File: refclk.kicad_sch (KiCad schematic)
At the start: 57 parts, among them J10 U.FL-R, Q1 PMOS Si2343DS, Q2 MMBT3904, Q3 PMOS Si2343DS, U14 LP5907MFX-3.3, U16 TLV3501, U18 NC7SV157, U19 74LVC2G14, U20 Si5351A, U21 NC7SV157, U22 SN65LVDS1, X1 TCXO-27M

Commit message: Bring over ringof/dev (tranche 2, stage 1): design, library, 3D, board CI & docs
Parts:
- C62, C65: footprint TIS_Footprints:PAD_0603 -> Library:C_0603
- C63, C64, C66, C67, C68, C69, C70, C71, C72, C73, C74, C75, C76: footprint TIS_Footprints:C_0603 -> Library:C_0603
- C78: footprint TIS_Footprints:PAD_0603 -> Library:C_0603; symbol capacitors:C-8.2p-0603 -> Library:C-8.2p-0603
- J10: footprint TIS_Footprints:HRS_U.FL-R-SMT(01) -> Library:HRS_U.FL-R-SMT(01)
- L15, L16, L17: footprint TIS_Footprints:0603 -> Library:0603
- Q1, Q2, Q3, U15, U17: footprint TIS_Footprints:SOT-23 -> Library:SOT-23
- R41, R42, R43, R44, R45, R46, R47, R48, R49, R50, R51, R52, R53, R54, R55, R56, R57, R60: footprint TIS_Footprints:PAD_0603 -> Library:PAD_0603
- R61: footprint TIS_Footprints:PAD_0603 -> Library:PAD_0603; symbol resistors:R-100-0603 -> Library:R-100-0603
- TP15, TP16, TP17, TP18, TP19: footprint TIS_Footprints:TP -> Library:TP; now not fitted
- U14, U22: footprint TIS_Footprints:SOT-23-5 -> Library:SOT-23-5
- U16: footprint TIS_Footprints:SOT-23-6 -> Library:SOT-23-6
- U18, U21: footprint TIS_Footprints:SC-70-6 -> Library:SC-70-6
- U19: footprint TIS_Footprints:SC-70-6_rot90 -> Library:SC-70-6_rot90
- U20: footprint TIS_Footprints:MSOP-10_W3mm -> Library:MSOP-10_W3mm
- X1: footprint TIS_Footprints:TCXO-3225 -> Library:TCXO-3225
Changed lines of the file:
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@@
 			)
 		)
-		(property "Footprint" "TIS_Footprints:SOT-23"
+		(property "Footprint" "Library:SOT-23"
 			(at 109.855 34.29 0)
 			(hide yes)
@@
 			)
 		)
-		(property "Footprint" "TIS_Footprints:SOT-23-6"
+		(property "Footprint" "Library:SOT-23-6"
 			(at 111.76 88.9 0)
 			(hide yes)
@@
 		(on_board yes)
 		(in_pos_files yes)
-		(dnp no)
+		(dnp yes)
 		(property "Reference" "TP17"
 			(at 90.3732 168.148 0)
@@
 			)
 		)
-		(property "Footprint" "TIS_Footprints:TP"
+		(property "Footprint" "Library:TP"
 			(at 85.09 161.29 0)
 			(hide yes)
@@
 			)
 		)
-		(property "Footprint" "TIS_Footprints:C_0603"
+		(property "Footprint" "Library:C_0603"
 			(at 138.176 39.878 0)
 			(hide yes)
@@
 			)
 		)
-		(property "Footprint" "TIS_Footprints:SOT-23-5"
+		(property "Footprint" "Library:SOT-23-5"
 			(at 234.95 52.07 0)
 			(hide yes)
@@
 			)
 		)
-		(property "Footprint" "TIS_Footprints:HRS_U.FL-R-SMT(01)"
+		(property "Footprint" "Library:HRS_U.FL-R-SMT(01)"
 			(at 219.71 10.16 0)
 			(hide yes)
@@
 			)
 		)
-		(property "Footprint" "TIS_Footprints:TCXO-3225"
+		(property "Footprint" "Library:TCXO-3225"
 			(at 153.67 58.42 0)
 			(hide yes)
@@
 			)
 		)
-		(property "Footprint" "TIS_Footprints:0603"
+		(property "Footprint" "Library:0603"
 			(at 128.778 27.178 0)
 			(hide yes)
@@
 			)
 		)
-		(property "Footprint" "TIS_Footprints:PAD_0603"
+		(property "Footprint" "Library:PAD_0603"
 			(at 173.736 120.904 90)
 			(hide yes)
@@
 			)
 		)
-		(property "Footprint" "TIS_Footprints:C_0603"
+		(property "Footprint" "Library:C_0603"
 			(at 189.484 79.502 0)
 			(hide yes)
@@
 			)
 		)
-		(property "Footprint" "TIS_Footprints:C_0603"
+		(property "Footprint" "Library:C_0603"
 			(at 205.994 141.732 0)
 			(hide yes)
@@
 	)
 	(symbol
-		(lib_id "resistors:R-100-0603")
+		(lib_id "Library:R-100-0603")
 		(at 246.38 29.21 0)
 		(unit 1)
@@
 			)
 		)
-		(property "Footprint" "TIS_Footprints:PAD_0603"
+		(property "Footprint" "Library:PAD_0603"
 			(at 247.396 29.464 90)
 			(hide yes)
@@
 			)
 		)
-		(property "Footprint" "TIS_Footprints:SOT-23"
+		(property "Footprint" "Library:SOT-23"
 			(at 58.928 123.317 0)
 			(hide yes)
@@
 			)
 		)
-		(property "Footprint" "TIS_Footprints:C_0603"
+		(property "Footprint" "Library:C_0603"
 			(at 232.156 112.268 0)
 			(hide yes)
@@
 			)
 		)
-		(property "Footprint" "TIS_Footprints:C_0603"
+		(property "Footprint" "Library:C_0603"
 			(at 241.554 49.022 0)
 			(hide yes)
@@
 			)
 		)
-		(property "Footprint" "TIS_Footprints:SOT-23"
+		(property "Footprint" "Library:SOT-23"
 			(at 132.588 141.097 0)
 			(hide yes)
@@
 			)
 		)
-		(property "Footprint" "TIS_Footprints:PAD_0603"
+		(property "Footprint" "Library:PAD_0603"
 			(at 218.186 90.424 90)
 			(hide yes)
@@
 			)
 		)
-		(property "Footprint" "TIS_Footprints:PAD_0603"
+		(property "Footprint" "Library:PAD_0603"
 			(at 232.156 156.464 90)
 			(hide yes)
@@
 			)
 		)
-		(property "Footprint" "TIS_Footprints:C_0603"
+		(property "Footprint" "Library:C_0603"
 			(at 254.254 144.272 0)
 			(hide yes)
@@
 		(on_board yes)
 		(in_pos_files yes)
-		(dnp no)
+		(dnp yes)
 		(property "Reference" "TP15"
 			(at 29.718 106.426 0)
@@
 			)
 		)
-		(property "Footprint" "TIS_Footprints:TP"
+		(property "Footprint" "Library:TP"
 			(at 26.67 100.33 0)
 			(hide yes)
@@
 			)
 		)
-		(property "Footprint" "TIS_Footprints:0603"
+		(property "Footprint" "Library:0603"
 			(at 222.758 99.568 0)
 			(hide yes)
@@
 			)
 		)
-		(property "Footprint" "TIS_Footprints:C_0603"
+		(property "Footprint" "Library:C_0603"
 			(at 131.318 131.064 0)
 			(hide yes)
@@
 			)
 		)
-		(property "Footprint" "TIS_Footprints:0603"
+		(property "Footprint" "Library:0603"
 			(at 44.958 46.228 0)
 			(hide yes)
@@
 		(on_board yes)
 		(in_pos_files yes)
-		(dnp no)
+		(dnp yes)
 		(property "Reference" "TP16"
 			(at 29.718 110.998 0)
@@
 			)
 		)
-		(property "Footprint" "TIS_Footprints:TP"
+		(property "Footprint" "Library:TP"
 			(at 26.67 104.14 0)
 			(hide yes)
@@
 			)
 		)
-		(property "Footprint" "TIS_Footprints:SC-70-6"
+		(property "Footprint" "Library:SC-70-6"
 			(at 240.03 148.59 0)
 			(hide yes)
@@
 			)
 		)
-		(property "Footprint" "TIS_Footprints:PAD_0603"
+		(property "Footprint" "Library:PAD_0603"
 			(at 79.756 76.454 90)
 			(hide yes)
@@
 			)
 		)
-		(property "Footprint" "TIS_Footprints:PAD_0603"
+		(property "Footprint" "Library:PAD_0603"
 			(at 152.146 139.954 90)
 			(hide yes)
@@
 			)
 		)
-		(property "Footprint" "TIS_Footprints:SC-70-6"
+		(property "Footprint" "Library:SC-70-6"
 			(at 177.8 78.74 0)
 			(hide yes)
@@
 			)
 		)
-		(property "Footprint" "TIS_Footprints:PAD_0603"
+		(property "Footprint" "Library:PAD_0603"
 			(at 79.756 61.214 90)
 			(hide yes)
@@
 			)
 		)
-		(property "Footprint" "TIS_Footprints:PAD_0603"
+		(property "Footprint" "Library:PAD_0603"
 			(at 251.206 61.214 90)
 			(hide yes)
@@
 			)
 		)
-		(property "Footprint" "TIS_Footprints:PAD_0603"
+		(property "Footprint" "Library:PAD_0603"
 			(at 38.354 155.194 90)
 			(hide yes)
@@
 		(on_board yes)
 		(in_pos_files yes)
-		(dnp no)
+		(dnp yes)
 		(property "Reference" "TP19"
 			(at 133.5532 110.998 0)
@@
 			)
 		)
-		(property "Footprint" "TIS_Footprints:TP"
+		(property "Footprint" "Library:TP"
 			(at 128.27 104.14 0)
 			(hide yes)
@@
 			)
 		)
-		(property "Footprint" "TIS_Footprints:SOT-23-5"
+		(property "Footprint" "Library:SOT-23-5"
 			(at 53.34 165.1 0)
 			(hide yes)
@@
 			)
 		)
-		(property "Footprint" "TIS_Footprints:PAD_0603"
+		(property "Footprint" "Library:PAD_0603"
 			(at 45.466 106.934 90)
 			(hide yes)
@@
 			)
 		)
-		(property "Footprint" "TIS_Footprints:PAD_0603"
+		(property "Footprint" "Library:PAD_0603"
 			(at 158.496 134.366 90)
 			(hide yes)
@@
 			)
 		)
-		(property "Footprint" "TIS_Footprints:SC-70-6_rot90"
+		(property "Footprint" "Library:SC-70-6_rot90"
 			(at 198.12 140.97 0)
 			(hide yes)
@@
 			)
 		)
-		(property "Footprint" "TIS_Footprints:PAD_0603"
+		(property "Footprint" "Library:PAD_0603"
 			(at 64.516 80.264 90)
 			(hide yes)
@@
 			)
 		)
-		(property "Footprint" "TIS_Footprints:PAD_0603"
+		(property "Footprint" "Library:PAD_0603"
 			(at 228.346 25.654 90)
 			(hide yes)
@@
 			)
 		)
-		(property "Footprint" "TIS_Footprints:C_0603"
+		(property "Footprint" "Library:C_0603"
 			(at 54.356 58.928 0)
 			(hide yes)
@@
 			)
 		)
-		(property "Footprint" "TIS_Footprints:PAD_0603"
+		(property "Footprint" "Library:C_0603"
 			(at 68.834 174.752 0)
 			(hide yes)
@@
 			)
 		)
-		(property "Footprint" "TIS_Footprints:C_0603"
+		(property "Footprint" "Library:C_0603"
 			(at 85.344 73.152 0)
 			(hide yes)
@@
 			)
 		)
-		(property "Footprint" "TIS_Footprints:PAD_0603"
+		(property "Footprint" "Library:PAD_0603"
 			(at 88.646 102.616 90)
 			(hide yes)
@@
 	)
 	(symbol
-		(lib_id "capacitors:C-8.2p-0603")
+		(lib_id "Library:C-8.2p-0603")
 		(at 266.7 29.21 0)
 		(unit 1)
@@
 			)
 		)
-		(property "Footprint" "TIS_Footprints:PAD_0603"
+		(property "Footprint" "Library:C_0603"
 			(at 265.684 20.574 0)
 			(hide yes)
@@
 			)
 		)
-		(property "Footprint" "TIS_Footprints:C_0603"
+		(property "Footprint" "Library:C_0603"
 			(at 92.964 112.522 0)
 			(hide yes)
@@
 			)
 		)
-		(property "Footprint" "TIS_Footprints:PAD_0603"
+		(property "Footprint" "Library:PAD_0603"
 			(at 64.516 37.084 90)
 			(hide yes)
@@
 			)
 		)
-		(property "Footprint" "TIS_Footprints:SOT-23"
+		(property "Footprint" "Library:SOT-23"
 			(at 64.135 19.05 0)
 			(hide yes)
@@
 			)
 		)
-		(property "Footprint" "TIS_Footprints:PAD_0603"
+		(property "Footprint" "Library:PAD_0603"
 			(at 40.386 106.934 90)
 			(hide yes)
@@
 			)
 		)
-		(property "Footprint" "TIS_Footprints:C_0603"
+		(property "Footprint" "Library:C_0603"
 			(at 53.848 99.314 0)
 			(hide yes)
@@
 			)
 		)
-		(property "Footprint" "TIS_Footprints:PAD_0603"
+		(property "Footprint" "Library:PAD_0603"
 			(at 73.406 102.616 90)
 			(hide yes)
@@
 			)
 		)
-		(property "Footprint" "TIS_Footprints:SOT-23"
+		(property "Footprint" "Library:SOT-23"
 			(at 175.26 135.255 0)
 			(hide yes)
@@
 		(on_board yes)
 		(in_pos_files yes)
-		(dnp no)
+		(dnp yes)
 		(property "Reference" "TP18"
 			(at 133.5532 107.188 0)
@@
 			)
 		)
-		(property "Footprint" "TIS_Footprints:TP"
+		(property "Footprint" "Library:TP"
 			(at 128.27 100.33 0)
 			(hide yes)
@@
 			)
 		)
-		(property "Footprint" "TIS_Footprints:PAD_0603"
+		(property "Footprint" "Library:PAD_0603"
 			(at 96.266 86.614 90)
 			(hide yes)
@@
 			)
 		)
-		(property "Footprint" "TIS_Footprints:C_0603"
+		(property "Footprint" "Library:C_0603"
 			(at 181.864 145.542 0)
 			(hide yes)
@@
 			)
 		)
-		(property "Footprint" "TIS_Footprints:PAD_0603"
+		(property "Footprint" "Library:PAD_0603"
 			(at 211.836 90.424 90)
 			(hide yes)
@@
 			)
 		)
-		(property "Footprint" "TIS_Footprints:MSOP-10_W3mm"
+		(property "Footprint" "Library:MSOP-10_W3mm"
 			(at 231.14 85.09 0)
 			(hide yes)
@@
 			)
 		)
-		(property "Footprint" "TIS_Footprints:PAD_0603"
+		(property "Footprint" "Library:C_0603"
 			(at 46.736 171.704 0)
 			(hide yes)
@@
 			)
 		)
-		(property "Footprint" "TIS_Footprints:C_0603"
+		(property "Footprint" "Library:C_0603"
 			(at 246.126 112.268 0)
 			(hide yes)

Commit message: fix BAV99 value, TIS exclude from BOM
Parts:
- U15, U17: value (none) -> BAV99
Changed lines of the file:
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@@
 			)
 		)
-		(property "Value" ""
+		(property "Value" "BAV99"
 			(at 60.96 124.3965 90)
 			(show_name no)
@@
 			)
 		)
-		(property "Value" ""
+		(property "Value" "BAV99"
 			(at 134.62 142.1765 90)
 			(show_name no)

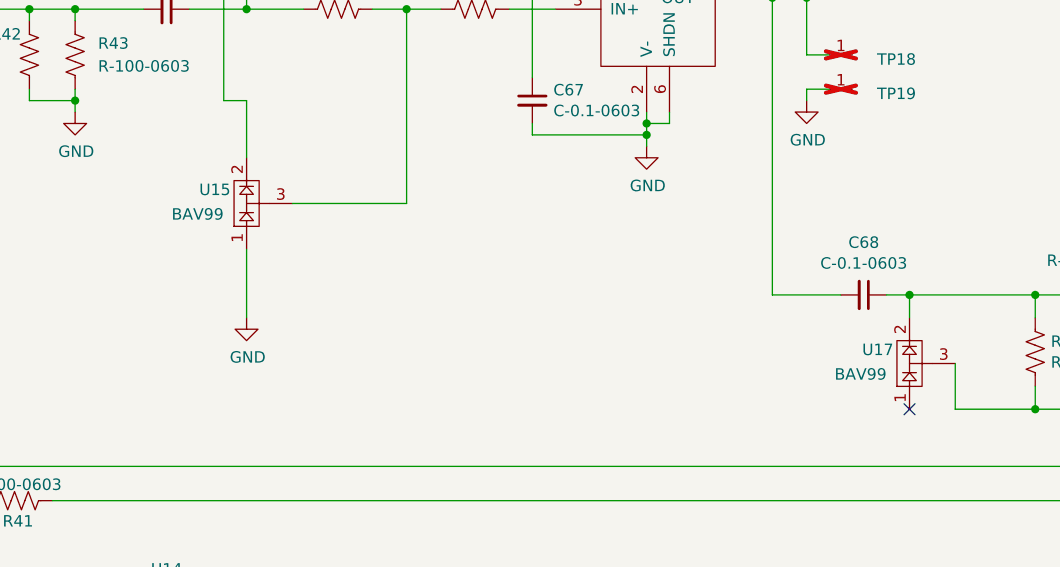
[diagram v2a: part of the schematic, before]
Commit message: Reconcile library/schematic/board drift (ERC/DRC clean at full severity)
Full-severity ERC/DRC surfaced 22 lib_symbol_mismatch + 5 lib_footprint_mismatch
warnings from cached copies drifting off the library master. Reconciled and
verified against the schematic and board:

- Symbol caches: refresh 8 cap/diode symbols whose embedded footprint field was
  stale (PAD_0603 -> C_0603); instances and PCB already used C_0603.
- SMA (J1-J4): push the board's tuned 3D-model offset/rotate into the library
  master and re-save it in KiCad 10 format; fix J1 LCSC C2874826 -> C914558 in
  schematic and board (J1 was an error, not a variant).
- U.FL (J10): re-save library footprint in v10 to match the routed board.

Result: ERC 0, DRC 0 (errors + warnings).
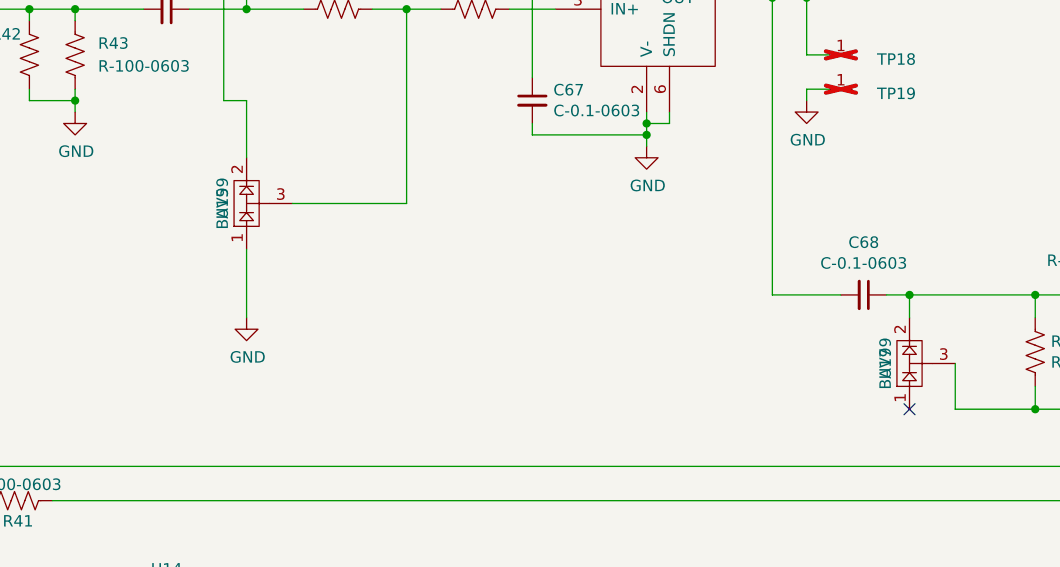
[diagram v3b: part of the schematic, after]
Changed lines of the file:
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@@
 		(dnp no)
 		(property "Reference" "U15"
-			(at 61.722 121.666 90)
-			(show_name no)
-			(do_not_autoplace no)
-			(effects
-				(font
-					(size 1.27 1.27)
-				)
-				(justify left)
+			(at 60.833 123.19 0)
+			(show_name no)
+			(do_not_autoplace no)
+			(effects
+				(font
+					(size 1.27 1.27)
+				)
 			)
 		)
 		(property "Value" "BAV99"
-			(at 60.96 124.3965 90)
-			(show_name no)
-			(do_not_autoplace no)
-			(effects
-				(font
-					(size 1.27 1.27)
-				)
-				(justify left)
+			(at 60.833 123.19 0)
+			(show_name no)
+			(do_not_autoplace no)
+			(effects
+				(font
+					(size 1.27 1.27)
+				)
 			)
 		)
@@
 		(dnp no)
 		(property "Reference" "U17"
-			(at 135.382 139.446 90)
-			(show_name no)
-			(do_not_autoplace no)
-			(effects
-				(font
-					(size 1.27 1.27)
-				)
-				(justify left)
+			(at 134.493 140.97 0)
+			(show_name no)
+			(do_not_autoplace no)
+			(effects
+				(font
+					(size 1.27 1.27)
+				)
 			)
 		)
 		(property "Value" "BAV99"
-			(at 134.62 142.1765 90)
-			(show_name no)
-			(do_not_autoplace no)
-			(effects
-				(font
-					(size 1.27 1.27)
-				)
-				(justify left)
-			)
-		)
+			(at 134.493 140.97 0)
+			(show_name no)
+			(do_not_autoplace no)
+			(effects
+				(font
+					(size 1.27 1.27)
+				)
+			)
+		)

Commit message: fixed wonky 'DNP' usage for removing 3D models for TP, now they are just via TP
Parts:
- TP15, TP16, TP17, TP18, TP19: now fitted
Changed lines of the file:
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@@
 		(on_board yes)
 		(in_pos_files yes)
-		(dnp yes)
+		(dnp no)
 		(property "Reference" "TP17"
 			(at 90.3732 168.148 0)
@@
 		(on_board yes)
 		(in_pos_files yes)
-		(dnp yes)
+		(dnp no)
 		(property "Reference" "TP15"
 			(at 29.718 106.426 0)
@@
 		(on_board yes)
 		(in_pos_files yes)
-		(dnp yes)
+		(dnp no)
 		(property "Reference" "TP16"
 			(at 29.718 110.998 0)
@@
 		(on_board yes)
 		(in_pos_files yes)
-		(dnp yes)
+		(dnp no)
 		(property "Reference" "TP19"
 			(at 133.5532 110.998 0)
@@
 		(on_board yes)
 		(in_pos_files yes)
-		(dnp yes)
+		(dnp no)
 		(property "Reference" "TP18"
 			(at 133.5532 107.188 0)
